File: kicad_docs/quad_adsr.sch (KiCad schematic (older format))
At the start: 0 parts

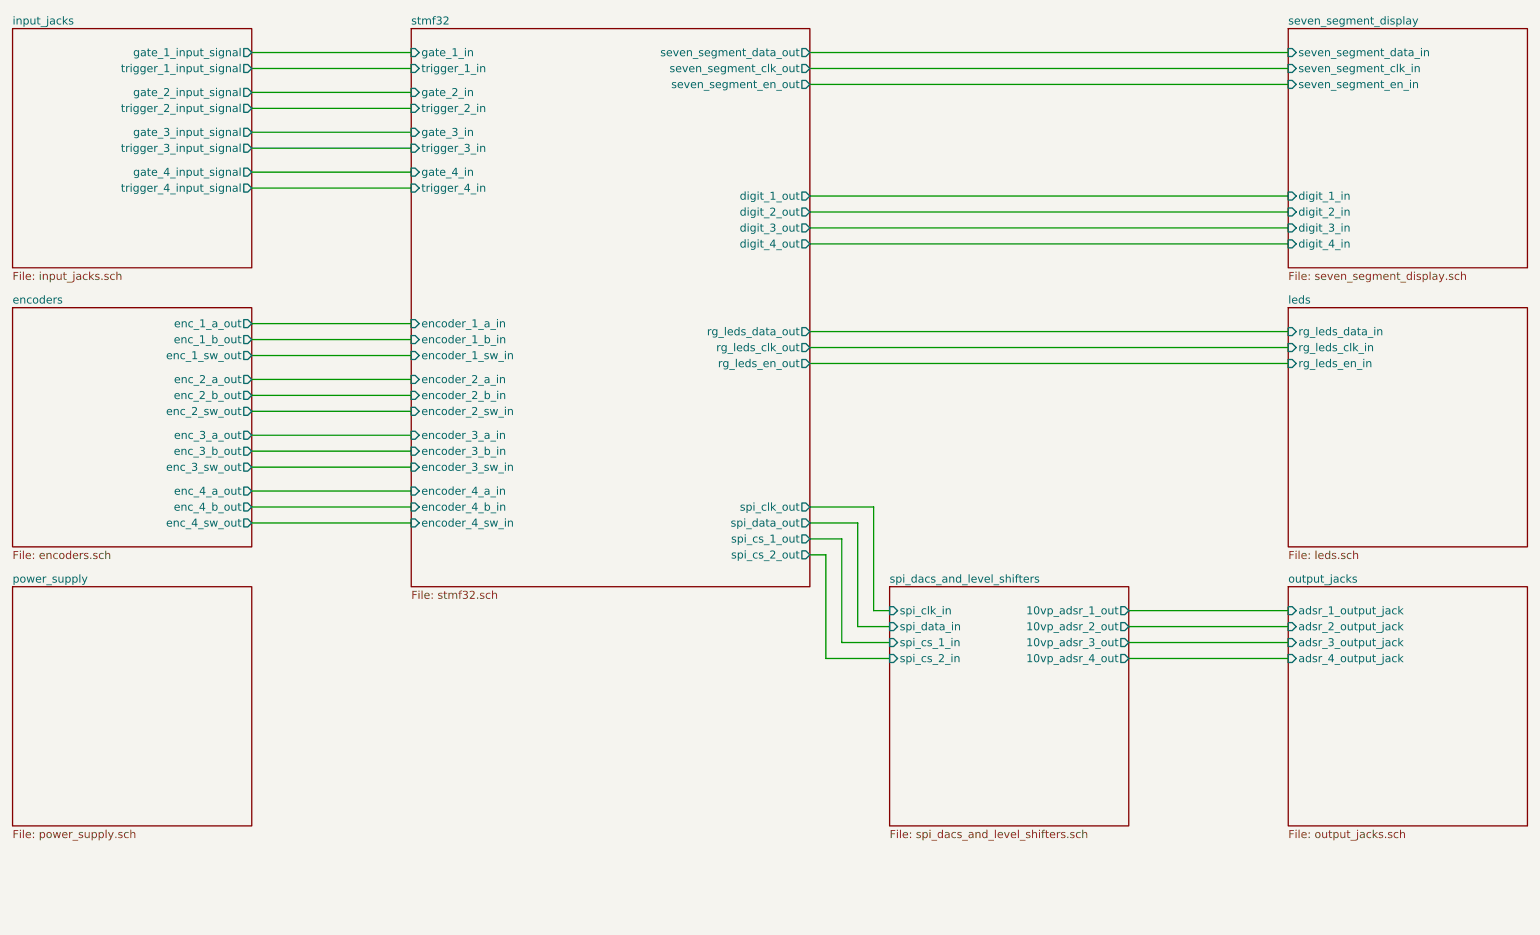
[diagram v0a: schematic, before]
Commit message: add EEPROM, big pcb re-design
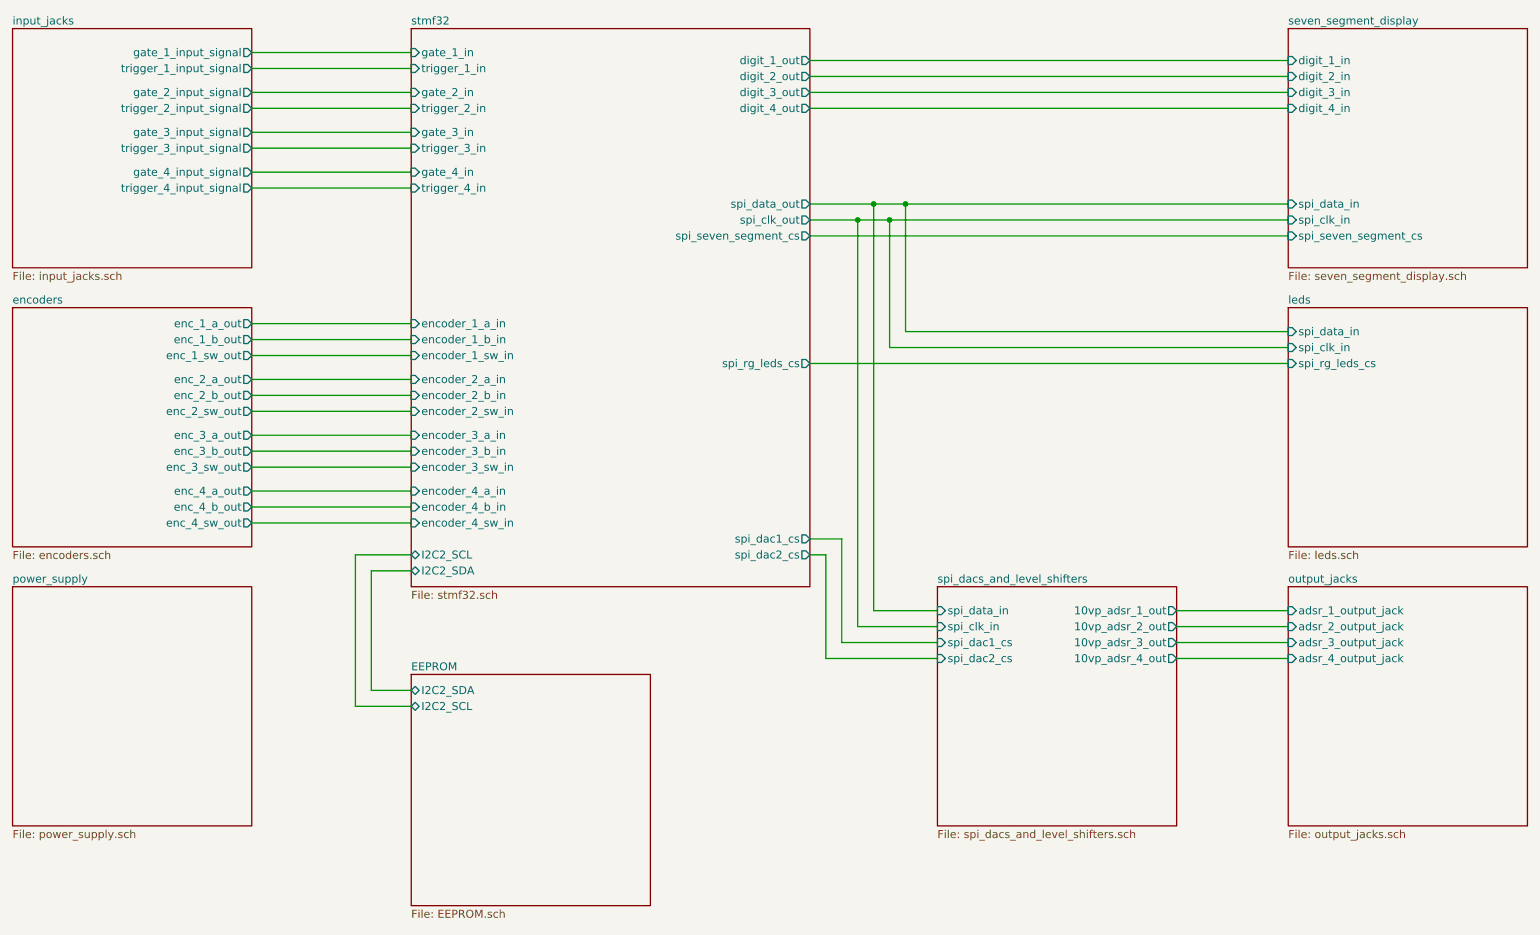
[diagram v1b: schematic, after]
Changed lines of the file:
@@
 $Descr A4 11693 8268
 encoding utf-8
-Sheet 1 9
+Sheet 1 10
 Title ""
 Date ""
@@
 F0 "seven_segment_display" 50
 F1 "seven_segment_display.sch" 50
-F2 "digit_1_in" I L 9000 2050 50
-F3 "digit_2_in" I L 9000 2150 50
-F4 "digit_3_in" I L 9000 2250 50
-F5 "digit_4_in" I L 9000 2350 50
-F6 "seven_segment_data_in" I L 9000 1150 50
-F7 "seven_segment_clk_in" I L 9000 1250 50
-F8 "seven_segment_en_in" I L 9000 1350 50
-$EndSheet
-$Sheet
-S 9000 2750 1500 1500
-U 5E63B0C2
-F0 "leds" 50
-F1 "leds.sch" 50
-F2 "rg_leds_data_in" I L 9000 2900 50
-F3 "rg_leds_clk_in" I L 9000 3000 50
-F4 "rg_leds_en_in" I L 9000 3100 50
+F2 "digit_1_in" I L 9000 1200 50
+F3 "digit_2_in" I L 9000 1300 50
+F4 "digit_3_in" I L 9000 1400 50
+F5 "digit_4_in" I L 9000 1500 50
+F6 "spi_data_in" I L 9000 2100 50
+F7 "spi_clk_in" I L 9000 2200 50
+F8 "spi_seven_segment_cs" I L 9000 2300 50
 $EndSheet
 $Sheet
@@
 	2500 4100 3500 4100
 Wire Wire Line
-	9000 2050 6000 2050
-Wire Wire Line
-	9000 2150 6000 2150
-Wire Wire Line
-	6000 2250 9000 2250
-Wire Wire Line
-	9000 2350 6000 2350
-Wire Wire Line
-	6000 4000 6400 4000
-Wire Wire Line
-	6400 4000 6400 4650
-Wire Wire Line
-	6400 4650 6500 4650
-Wire Wire Line
-	6500 4750 6300 4750
-Wire Wire Line
-	6300 4750 6300 4100
-Wire Wire Line
-	6300 4100 6000 4100
-Wire Wire Line
-	6500 4850 6200 4850
+	6800 4850 6200 4850
 Wire Wire Line
 	6200 4850 6200 4200
 Wire Wire Line
-	6200 4200 6000 4200
-Wire Wire Line
-	6500 4950 6100 4950
+	6800 4950 6100 4950
 Wire Wire Line
 	6100 4950 6100 4300
 Wire Wire Line
-	6100 4300 6000 4300
-Wire Wire Line
-	8000 4650 9000 4650
-Wire Wire Line
-	9000 4750 8000 4750
-Wire Wire Line
-	8000 4850 9000 4850
-Wire Wire Line
-	9000 4950 8000 4950
+	8300 4650 9000 4650
+Wire Wire Line
+	9000 4750 8300 4750
+Wire Wire Line
+	8300 4850 9000 4850
+Wire Wire Line
+	9000 4950 8300 4950
 $Sheet
 S 1000 1000 1500 1500
@@
 $EndSheet
 $Sheet
-S 6500 4500 1500 1500
-U 5E595FD4
-F0 "spi_dacs_and_level_shifters" 50
-F1 "spi_dacs_and_level_shifters.sch" 50
-F2 "spi_clk_in" I L 6500 4650 50
-F3 "spi_data_in" I L 6500 4750 50
-F4 "spi_cs_1_in" I L 6500 4850 50
-F5 "spi_cs_2_in" I L 6500 4950 50
-F6 "10vp_adsr_1_out" O R 8000 4650 50
-F7 "10vp_adsr_2_out" O R 8000 4750 50
-F8 "10vp_adsr_3_out" O R 8000 4850 50
-F9 "10vp_adsr_4_out" O R 8000 4950 50
-$EndSheet
-Wire Wire Line
-	6000 1150 9000 1150
-Wire Wire Line
-	9000 1250 6000 1250
+S 3500 5050 1500 1450
+U 5EE2D7E5
+F0 "EEPROM" 50
+F1 "EEPROM.sch" 50
+F2 "I2C2_SDA" B L 3500 5150 50
+F3 "I2C2_SCL" B L 3500 5250 50
+$EndSheet
 $Sheet
 S 3500 1000 2500 3500
@@
 F20 "encoder_4_b_in" I L 3500 4000 50
 F21 "encoder_4_sw_in" I L 3500 4100 50
-F22 "digit_1_out" O R 6000 2050 50
-F23 "digit_2_out" O R 6000 2150 50
-F24 "digit_3_out" O R 6000 2250 50
-F25 "digit_4_out" O R 6000 2350 50
-F26 "spi_clk_out" O R 6000 4000 50
-F27 "spi_data_out" O R 6000 4100 50
-F28 "spi_cs_1_out" O R 6000 4200 50
-F29 "spi_cs_2_out" O R 6000 4300 50
-F30 "seven_segment_data_out" O R 6000 1150 50
-F31 "seven_segment_clk_out" O R 6000 1250 50
-F32 "rg_leds_data_out" O R 6000 2900 50
-F33 "rg_leds_clk_out" O R 6000 3000 50
-F34 "seven_segment_en_out" O R 6000 1350 50
-F35 "rg_leds_en_out" O R 6000 3100 50
-$EndSheet
-Wire Wire Line
-	6000 2900 9000 2900
-Wire Wire Line
-	9000 3000 6000 3000
+F22 "digit_1_out" O R 6000 1200 50
+F23 "digit_2_out" O R 6000 1300 50
+F24 "digit_3_out" O R 6000 1400 50
+F25 "digit_4_out" O R 6000 1500 50
+F26 "I2C2_SCL" B L 3500 4300 50
+F27 "I2C2_SDA" B L 3500 4400 50
+F28 "spi_clk_out" O R 6000 2200 50
+F29 "spi_data_out" O R 6000 2100 50
+F30 "spi_dac1_cs" O R 6000 4200 50
+F31 "spi_dac2_cs" O R 6000 4300 50
+F32 "spi_seven_segment_cs" O R 6000 2300 50
+F33 "spi_rg_leds_cs" O R 6000 3100 50
+$EndSheet
+Wire Wire Line
+	3500 4400 3250 4400
+Wire Wire Line
+	3250 4400 3250 5150
+Wire Wire Line
+	3250 5150 3500 5150
+Wire Wire Line
+	3500 5250 3150 5250
+Wire Wire Line
+	3150 5250 3150 4300
+Wire Wire Line
+	3150 4300 3500 4300
 Wire Wire Line
 	9000 3100 6000 3100
 Wire Wire Line
-	9000 1350 6000 1350
+	6100 4300 6000 4300
+Wire Wire Line
+	6000 4200 6200 4200
+Wire Wire Line
+	9000 2900 6600 2900
+Wire Wire Line
+	6500 3000 9000 3000
+$Sheet
+S 6800 4500 1500 1500
+U 5E595FD4
+F0 "spi_dacs_and_level_shifters" 50
+F1 "spi_dacs_and_level_shifters.sch" 50
+F2 "10vp_adsr_1_out" O R 8300 4650 50
+F3 "10vp_adsr_2_out" O R 8300 4750 50
+F4 "10vp_adsr_3_out" O R 8300 4850 50
+F5 "10vp_adsr_4_out" O R 8300 4950 50
+F6 "spi_data_in" I L 6800 4650 50
+F7 "spi_dac1_cs" I L 6800 4850 50
+F8 "spi_dac2_cs" I L 6800 4950 50
+F9 "spi_clk_in" I L 6800 4750 50
+$EndSheet
+Wire Wire Line
+	6800 4650 6400 4650
+Wire Wire Line
+	6300 4750 6800 4750
+$Sheet
+S 9000 2750 1500 1500
+U 5E63B0C2
+F0 "leds" 50
+F1 "leds.sch" 50
+F2 "spi_data_in" I L 9000 2900 50
+F3 "spi_clk_in" I L 9000 3000 50
+F4 "spi_rg_leds_cs" I L 9000 3100 50
+$EndSheet
+Wire Wire Line
+	9000 2300 6000 2300
+Wire Wire Line
+	9000 2200 6500 2200
+Wire Wire Line
+	6000 2100 6400 2100
+Wire Wire Line
+	6600 2900 6600 2100
+Connection ~ 6600 2100
+Wire Wire Line
+	6600 2100 9000 2100
+Wire Wire Line
+	6500 2200 6500 3000
+Connection ~ 6500 2200
+Wire Wire Line
+	6500 2200 6300 2200
+Wire Wire Line
+	6400 4650 6400 2100
+Connection ~ 6400 2100
+Wire Wire Line
+	6400 2100 6600 2100
+Wire Wire Line
+	6300 4750 6300 2200
+Connection ~ 6300 2200
+Wire Wire Line
+	6300 2200 6000 2200
+Wire Wire Line
+	6000 1200 9000 1200
+Wire Wire Line
+	6000 1300 9000 1300
+Wire Wire Line
+	9000 1400 6000 1400
+Wire Wire Line
+	6000 1500 9000 1500
 $EndSCHEMATC
